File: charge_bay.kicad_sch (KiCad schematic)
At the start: 94 parts, among them J1 USB_C_Receptacle_USB2.0, J10 Conn_01x03_Pin, J11 Conn_01x05_Socket, J2 Screw_Terminal_01x04, J3 Conn_01x03_Pin, J4 Conn_01x03_Pin, J6 Conn_01x05_Socket, J7 Screw_Terminal_01x04, J8 Conn_01x03_Pin, Q1 MMBT3904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

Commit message: Update to swap to basic for MMBT3904 transistors
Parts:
- Q1, Q2, Q3, Q4, Q5: JLCPCB C111113 -> C20526; JLCType Extended -> Basic
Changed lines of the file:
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@@
 			)
 		)
-		(property "JLCPCB" "C111113"
+		(property "JLCPCB" "C20526"
 			(at 43.18 17.78 0)
 			(effects
@@
 			)
 		)
-		(property "JLCType" "Extended"
+		(property "JLCType" "Basic"
 			(at 43.18 17.78 0)
 			(effects
@@
 			)
 		)
-		(property "JLCPCB" "C111113"
+		(property "JLCPCB" "C20526"
 			(at 53.34 17.78 0)
 			(effects
@@
 			)
 		)
-		(property "JLCType" "Extended"
+		(property "JLCType" "Basic"
 			(at 53.34 17.78 0)
 			(effects
@@
 			)
 		)
-		(property "JLCPCB" "C111113"
+		(property "JLCPCB" "C20526"
 			(at 33.02 17.78 0)
 			(effects
@@
 			)
 		)
-		(property "JLCType" "Extended"
+		(property "JLCType" "Basic"
 			(at 33.02 17.78 0)
 			(effects
@@
 			)
 		)
-		(property "JLCPCB" "C111113"
+		(property "JLCPCB" "C20526"
 			(at 22.86 17.78 0)
 			(effects
@@
 			)
 		)
-		(property "JLCType" "Extended"
+		(property "JLCType" "Basic"
 			(at 22.86 17.78 0)
 			(effects
@@
 			)
 		)
-		(property "JLCPCB" "C111113"
+		(property "JLCPCB" "C20526"
 			(at 12.7 17.78 0)
 			(effects
@@
 			)
 		)
-		(property "JLCType" "Extended"
+		(property "JLCType" "Basic"
 			(at 12.7 17.78 0)
 			(effects

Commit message: Adds Regulator & adjusts rotation on Y2, D24, U1, U2 & U5
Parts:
- U4: JLCPCB (none) -> C2876186; JLCType (none) -> Extended
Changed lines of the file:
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@@
+			)
+		)
+		(property "JLCPCB" "C2876186"
+			(at 25.4 153.67 0)
+			(effects
+				(font
+					(size 1.27 1.27)
+				)
+				(hide yes)
+			)
+		)
+		(property "JLCType" "Extended"
+			(at 25.4 153.67 0)
+			(effects
+				(font
+					(size 1.27 1.27)
+				)
+				(hide yes)
 			)
 		)

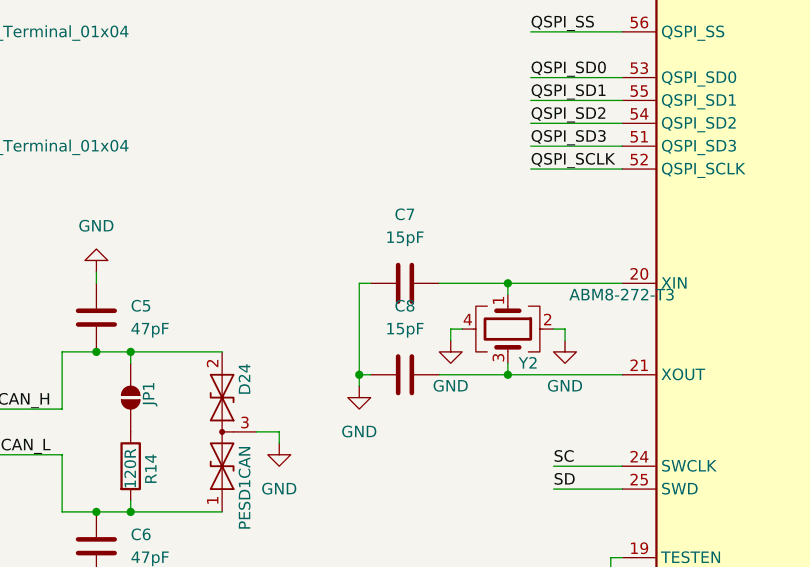
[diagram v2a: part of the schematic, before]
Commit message: Update Silkscreen With Pololu Parts, etc.
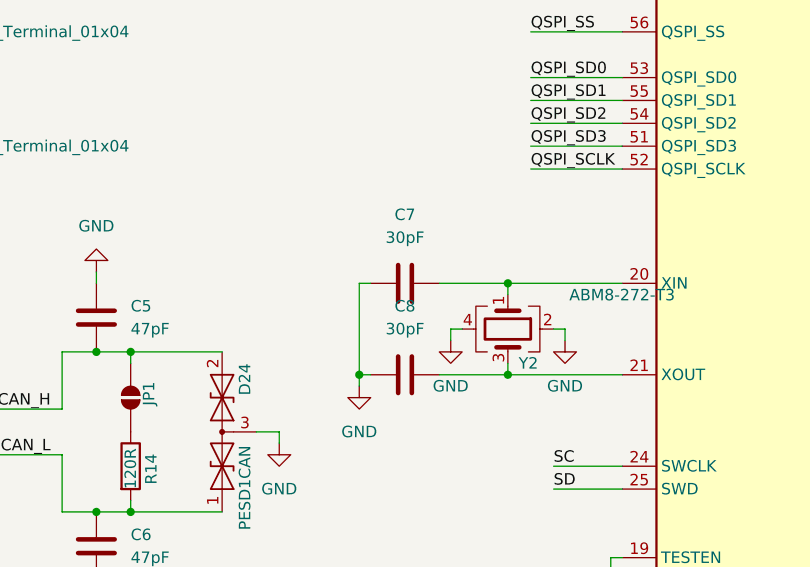
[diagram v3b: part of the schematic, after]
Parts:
- C7, C8: value 15pF -> 30pF; JLCPCB C1644 -> C1658
- Y2: JLCPCB C20625731 -> C9002; JLCType Extended -> Basic
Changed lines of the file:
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@@
 			)
 		)
-		(property "Datasheet" "~"
+		(property "Datasheet" "https://jlcpcb.com/partdetail/Yxc_CrystalOscillators-X322512MSB4SI/C9002"
 			(at 163.83 118.11 0)
 			(effects
@@
 			)
 		)
-		(property "JLCPCB" "C20625731"
+		(property "JLCPCB" "C9002"
 			(at 163.83 118.11 0)
 			(effects
@@
 			)
 		)
-		(property "JLCType" "Extended"
+		(property "JLCType" "Basic"
 			(at 163.83 118.11 0)
 			(effects
@@
 			)
 		)
-		(property "Value" "15pF"
+		(property "Value" "30pF"
 			(at 152.4 118.11 90)
 			(effects
@@
 			)
 		)
-		(property "JLCPCB" "C1644"
+		(property "JLCPCB" "C1658"
 			(at 152.4 123.19 90)
 			(effects
@@
 			)
 		)
-		(property "Value" "15pF"
+		(property "Value" "30pF"
 			(at 152.4 107.95 90)
 			(effects
@@
 			)
 		)
-		(property "JLCPCB" "C1644"
+		(property "JLCPCB" "C1658"
 			(at 152.4 113.03 90)
 			(effects
